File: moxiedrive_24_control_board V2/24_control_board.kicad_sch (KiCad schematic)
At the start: 32 parts, among them J101 Conn_01x03, P101 Conn_01x08, P102 Serial1/tim4, P103 I2C, P104 JST-PH, P105 JST-GH, P106 JST-GH Rev, SW101 SW_DIP_x04

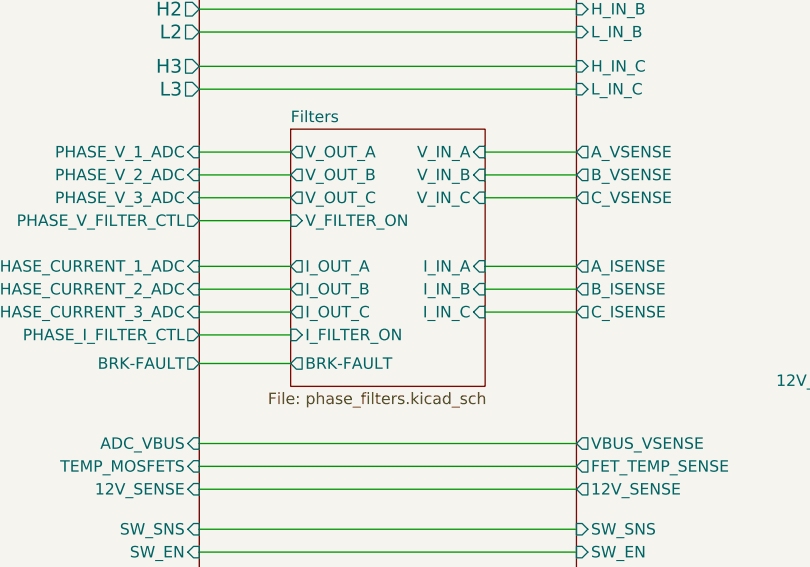
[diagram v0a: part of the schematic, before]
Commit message: fix misplaced component
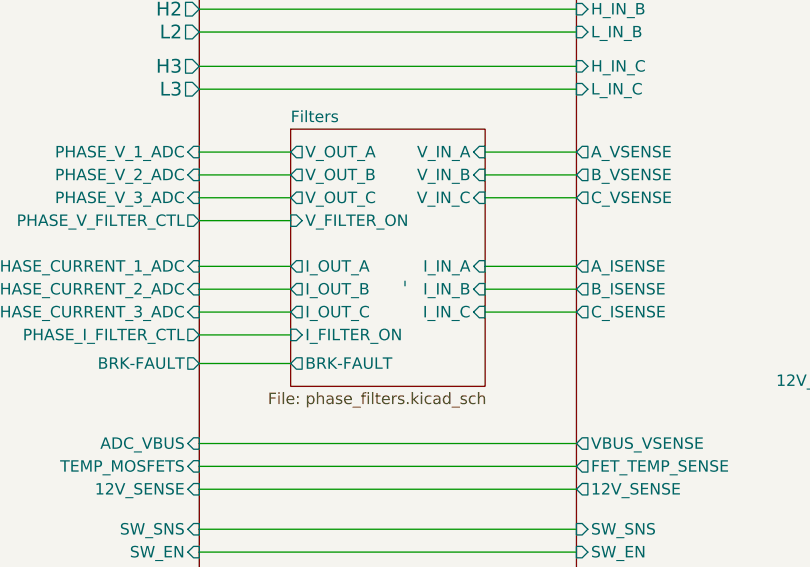
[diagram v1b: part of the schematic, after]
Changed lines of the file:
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@@
+    (stroke (width 0) (type default))
+  )
+  (bus (pts (xy 186.69 64.516) (xy 186.69 65.024))
     (stroke (width 0) (type default))
   )
